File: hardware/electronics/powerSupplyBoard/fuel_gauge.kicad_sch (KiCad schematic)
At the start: 20 parts, among them Q4 BSS84, Q5 2N7002, Q6 2N7002, U6 BQ34Z100-R2

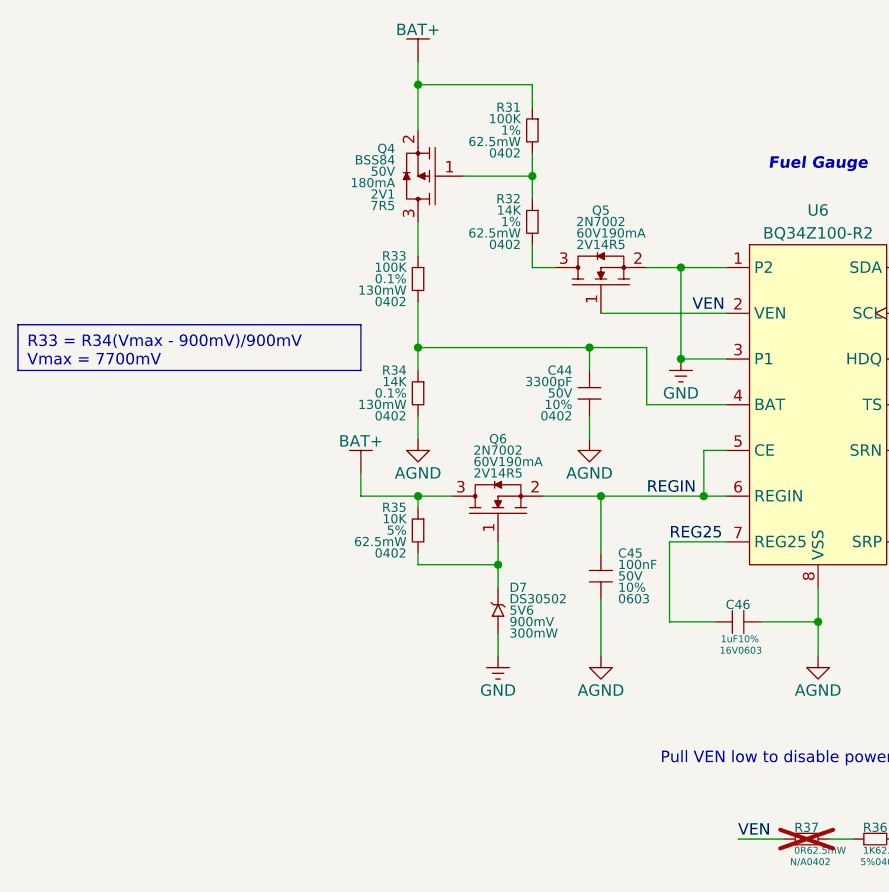
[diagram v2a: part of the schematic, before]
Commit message: added testpoints
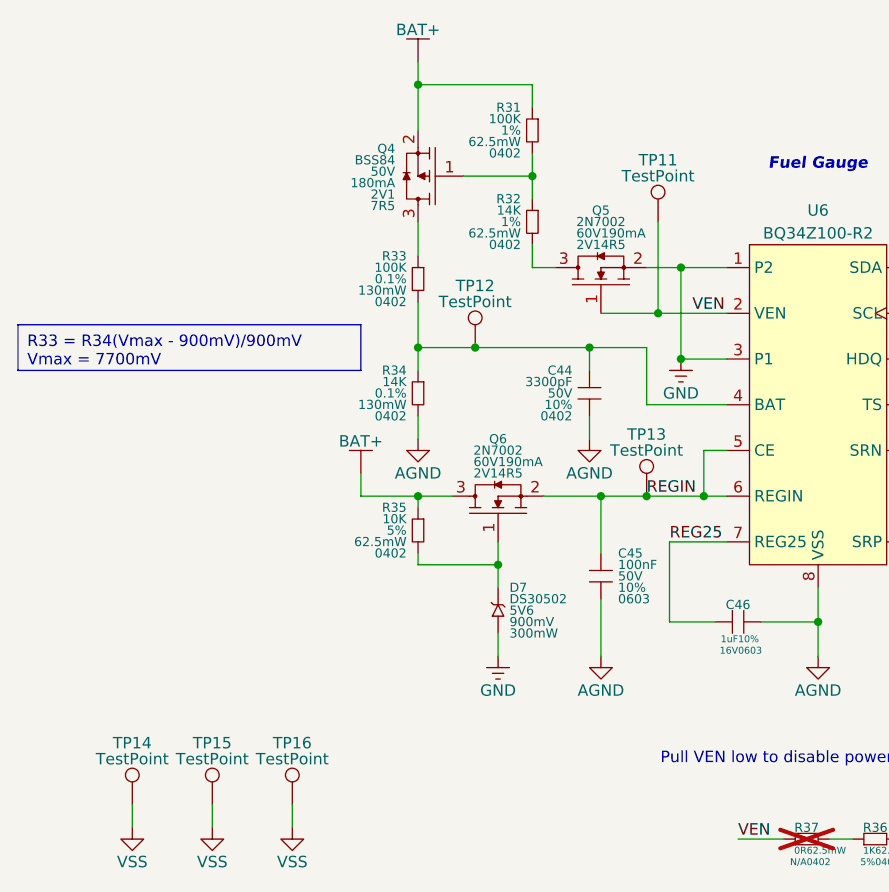
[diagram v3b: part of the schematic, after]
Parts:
- added TP11, TP12, TP13, TP14, TP15, TP16: TestPoint, lib_fp:TP_1mm, symbol lib_sch:TestPoint
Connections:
- net REGIN: now also TP13.1
- net VEN: now also TP11.1
- net at C44.1, R33.2, R34.1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: now also TP12.1
- new net VSS: TP14.1, TP15.1, TP16.1

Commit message: cleaned up schematics
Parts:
- C41, C42, C43, C44, C45: symbol lib_sch:C_2 -> lib_sch:C
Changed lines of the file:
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@@
 	(title_block
 		(title "LiFePO4 State of Charge")
-		(date "2024-11-18")
+		(date "2024-11-20")
 		(rev "01")
 		(comment 2 "PROTOTYPE")
@@
 	)
 	(symbol
-		(lib_name "C_2")
-		(lib_id "lib_sch:C_2")
+		(lib_id "lib_sch:C")
 		(at 165.1 129.54 0)
 		(unit 1)
@@
 	)
 	(symbol
-		(lib_name "C_2")
-		(lib_id "lib_sch:C_2")
+		(lib_id "lib_sch:C")
 		(at 152.4 118.11 0)
 		(unit 1)
@@
 	)
 	(symbol
-		(lib_name "C_2")
-		(lib_id "lib_sch:C_2")
+		(lib_id "lib_sch:C")
 		(at 115.57 127 0)
 		(unit 1)
@@
 	)
 	(symbol
-		(lib_name "C_2")
-		(lib_id "lib_sch:C_2")
+		(lib_id "lib_sch:C")
 		(at 175.26 129.54 0)
 		(unit 1)
@@
 	)
 	(symbol
-		(lib_name "C_2")
-		(lib_id "lib_sch:C_2")
+		(lib_id "lib_sch:C")
 		(at 114.3 106.68 0)
 		(mirror y)
